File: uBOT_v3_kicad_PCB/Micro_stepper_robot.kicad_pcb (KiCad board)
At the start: 2 copper layers, 37 x 47 mm, 29 parts, among them J4 USB_B_Micro, M1 Stepper_Motor_bipolar, M2 Stepper_Motor_bipolar, M3 Stepper_Motor_bipolar, M4 Stepper_Motor_bipolar, SW3 EN, SW4 BOOT, U1 DRV8833PW, U2 TCRT5000, U4 ESP32-WROOM-32D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

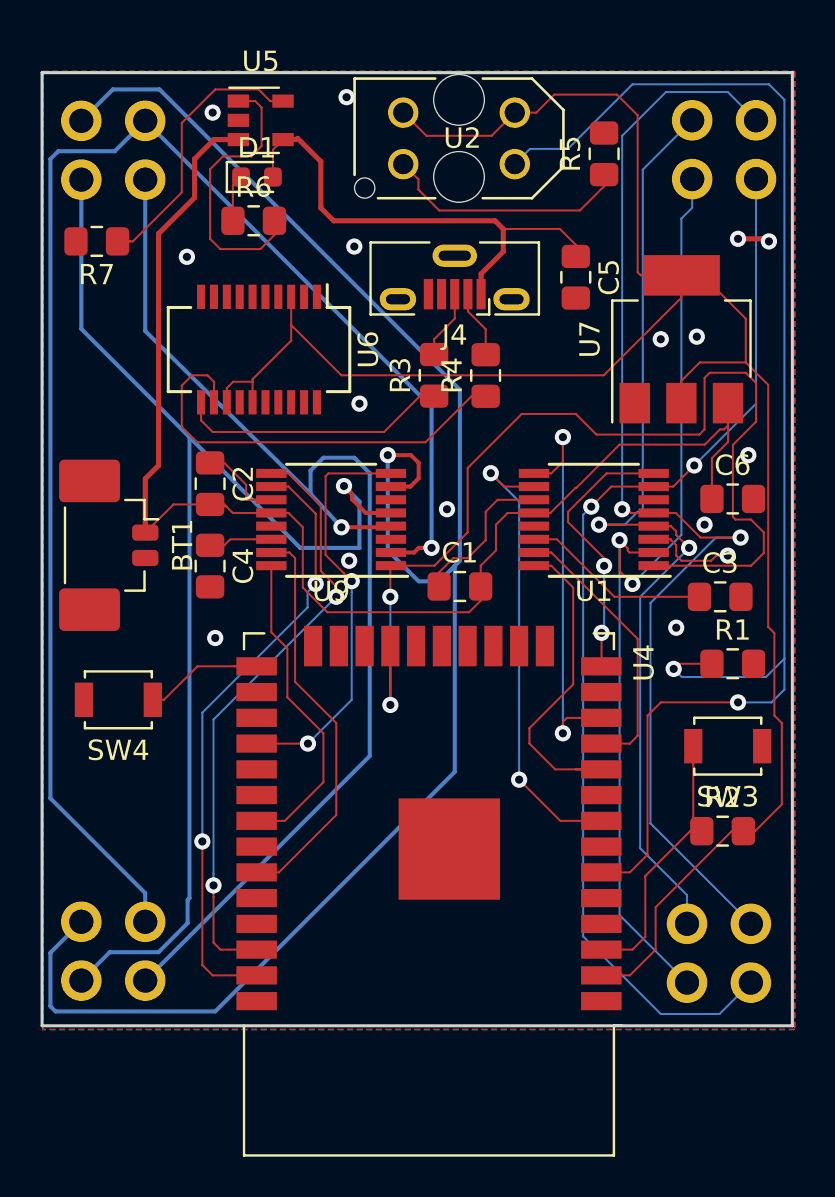
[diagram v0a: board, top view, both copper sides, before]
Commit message: added filter caps to 3.3v and VBAT
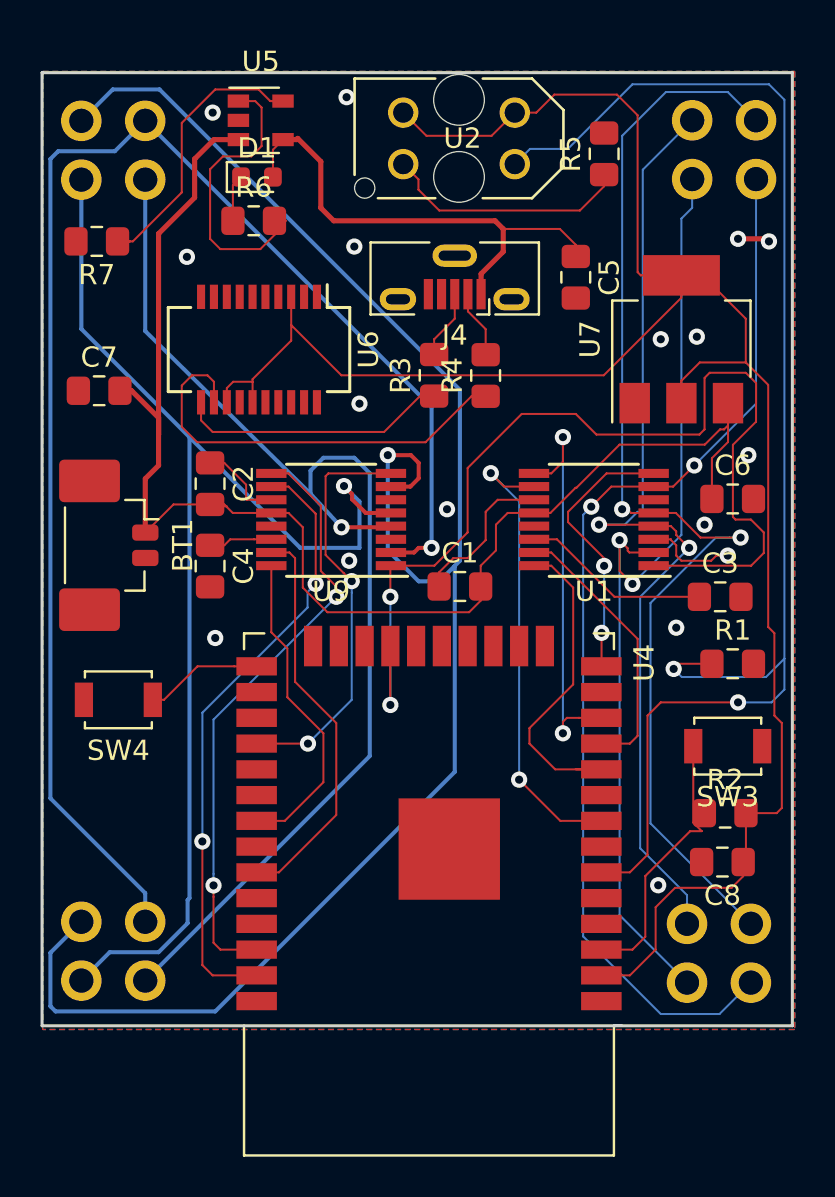
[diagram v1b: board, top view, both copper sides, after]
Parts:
- added C7: 10uF, Capacitor_SMD:C_0805_2012Metric_Pad1.15x1.40mm_HandSolder, F.Cu at (105.7, 68.3)
- added C8: 10uF, Capacitor_SMD:C_0805_2012Metric_Pad1.15x1.40mm_HandSolder, F.Cu at (136.4, 91.6)
- C3, C4: value C_Small -> 2.2uF
- moved R2 0.90 mm to (136.5, 89.2)
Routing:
- net +BATT: track 67.7 -> 71.0 mm
- net +3V3: track 101.3 -> 103.2 mm
- net GND: vias 16 -> 17
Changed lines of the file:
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@@
     (thickness 1.6)
     (drawings 5)
-    (tracks 467)
+    (tracks 476)
     (zones 0)
-    (modules 29)
+    (modules 31)
     (nets 73)
   )
@@
     (add_net "Net-(U6-Pad9)")
   )
+  (module Capacitor_SMD:C_0805_2012Metric_Pad1.15x1.40mm_HandSolder (layer F.Cu)
+    (at 136.389 91.567 180)
+    (descr "Capacitor SMD 0805 (2012 Metric), square (rectangular) end terminal, IPC_7351 nominal with elongated pad for handsoldering. (Body size source: https://docs.google.com/spreadsheets/d/1BsfQQcO9C6DZCsRaXUlFlo91Tg2WpOkGARC1WS5S8t0/edit?usp=sharing), generated with kicad-footprint-generator")
+    (tags "capacitor handsolder")
+    (attr smd)
+    (fp_text reference C8 (at 0 -1.65) (layer F.SilkS)
+      (effects (font (size 1 1) (thickness 0.15)))
+    )
+    (fp_text value 10uF (at 0 1.65) (layer F.Fab)
+      (effects (font (size 1 1) (thickness 0.15)))
+    )
+    (fp_text user %R (at 0 0) (layer F.Fab)
+      (effects (font (size 0.5 0.5) (thickness 0.08)))
+    )
+    (fp_line (start 1.85 0.95) (end -1.85 0.95) (layer F.CrtYd) (width 0.05))
+    (fp_line (start 1.85 -0.95) (end 1.85 0.95) (layer F.CrtYd) (width 0.05))
+    (fp_line (start -1.85 -0.95) (end 1.85 -0.95) (layer F.CrtYd) (width 0.05))
+    (fp_line (start -1.85 0.95) (end -1.85 -0.95) (layer F.CrtYd) (width 0.05))
+    (fp_line (start -0.261252 0.71) (end 0.261252 0.71) (layer F.SilkS) (width 0.12))
+    (fp_line (start -0.261252 -0.71) (end 0.261252 -0.71) (layer F.SilkS) (width 0.12))
+    (fp_line (start 1 0.6) (end -1 0.6) (layer F.Fab) (width 0.1))
+    (fp_line (start 1 -0.6) (end 1 0.6) (layer F.Fab) (width 0.1))
+    (fp_line (start -1 -0.6) (end 1 -0.6) (layer F.Fab) (width 0.1))
+    (fp_line (start -1 0.6) (end -1 -0.6) (layer F.Fab) (width 0.1))
+    (pad 2 smd roundrect (at 1.025 0 180) (size 1.15 1.4) (layers F.Cu F.Paste F.Mask) (roundrect_rratio 0.217391)
+      (net 5 GND))
+    (pad 1 smd roundrect (at -1.025 0 180) (size 1.15 1.4) (layers F.Cu F.Paste F.Mask) (roundrect_rratio 0.217391)
+      (net 22 +3V3))
+    (model ${KISYS3DMOD}/Capacitor_SMD.3dshapes/C_0805_2012Metric.wrl
+      (at (xyz 0 0 0))
+      (scale (xyz 1 1 1))
+      (rotate (xyz 0 0 0))
+    )
+  )
+  (module Capacitor_SMD:C_0805_2012Metric_Pad1.15x1.40mm_HandSolder (layer F.Cu)
+    (at 105.655 68.326)
+    (descr "Capacitor SMD 0805 (2012 Metric), square (rectangular) end terminal, IPC_7351 nominal with elongated pad for handsoldering. (Body size source: https://docs.google.com/spreadsheets/d/1BsfQQcO9C6DZCsRaXUlFlo91Tg2WpOkGARC1WS5S8t0/edit?usp=sharing), generated with kicad-footprint-generator")
+    (tags "capacitor handsolder")
+    (attr smd)
+    (fp_text reference C7 (at 0 -1.65) (layer F.SilkS)
+      (effects (font (size 1 1) (thickness 0.15)))
+    )
+    (fp_text value 10uF (at 0 1.65) (layer F.Fab)
+      (effects (font (size 1 1) (thickness 0.15)))
+    )
+    (fp_text user %R (at 0 0) (layer F.Fab)
+      (effects (font (size 0.5 0.5) (thickness 0.08)))
+    )
+    (fp_line (start 1.85 0.95) (end -1.85 0.95) (layer F.CrtYd) (width 0.05))
+    (fp_line (start 1.85 -0.95) (end 1.85 0.95) (layer F.CrtYd) (width 0.05))
+    (fp_line (start -1.85 -0.95) (end 1.85 -0.95) (layer F.CrtYd) (width 0.05))
+    (fp_line (start -1.85 0.95) (end -1.85 -0.95) (layer F.CrtYd) (width 0.05))
+    (fp_line (start -0.261252 0.71) (end 0.261252 0.71) (layer F.SilkS) (width 0.12))
+    (fp_line (start -0.261252 -0.71) (end 0.261252 -0.71) (layer F.SilkS) (width 0.12))
+    (fp_line (start 1 0.6) (end -1 0.6) (layer F.Fab) (width 0.1))
+    (fp_line (start 1 -0.6) (end 1 0.6) (layer F.Fab) (width 0.1))
+    (fp_line (start -1 -0.6) (end 1 -0.6) (layer F.Fab) (width 0.1))
+    (fp_line (start -1 0.6) (end -1 -0.6) (layer F.Fab) (width 0.1))
+    (pad 2 smd roundrect (at 1.025 0) (size 1.15 1.4) (layers F.Cu F.Paste F.Mask) (roundrect_rratio 0.217391)
+      (net 4 +BATT))
+    (pad 1 smd roundrect (at -1.025 0) (size 1.15 1.4) (layers F.Cu F.Paste F.Mask) (roundrect_rratio 0.217391)
+      (net 5 GND))
+    (model ${KISYS3DMOD}/Capacitor_SMD.3dshapes/C_0805_2012Metric.wrl
+      (at (xyz 0 0 0))
+      (scale (xyz 1 1 1))
+      (rotate (xyz 0 0 0))
+    )
+  )
   (module Connector_Molex:Molex_PicoBlade_53398-0271_1x02-1MP_P1.25mm_Vertical (layer F.Cu)
     (at 106.68 75.946 270)
@@
       (effects (font (size 1 1) (thickness 0.15)))
     )
-    (fp_text value C_Small (at 0 1.65) (layer F.Fab)
+    (fp_text value 2.2uF (at 0 1.65) (layer F.Fab)
       (effects (font (size 1 1) (thickness 0.15)))
     )
@@
       (effects (font (size 1 1) (thickness 0.15)))
     )
-    (fp_text value C_Small (at 0 1.65 90) (layer F.Fab)
+    (fp_text value 2.2uF (at 0 1.65 90) (layer F.Fab)
       (effects (font (size 1 1) (thickness 0.15)))
     )
@@
   )
   (module Resistor_SMD:R_0805_2012Metric_Pad1.15x1.40mm_HandSolder (layer F.Cu)
-    (at 136.398 90.043)
+    (at 136.525 89.154)
     (descr "Resistor SMD 0805 (2012 Metric), square (rectangular) end terminal, IPC_7351 nominal with elongated pad for handsoldering. (Body size source: https://docs.google.com/spreadsheets/d/1BsfQQcO9C6DZCsRaXUlFlo91Tg2WpOkGARC1WS5S8t0/edit?usp=sharing), generated with kicad-footprint-generator")
     (tags "resistor handsolder")
@@
   (segment (start 107.93 75.321) (end 107.93 72.664) (width 0.254) (layer F.Cu) (net 4))
   (segment (start 107.93 72.664) (end 108.585 72.009) (width 0.254) (layer F.Cu) (net 4))
-  (segment (start 108.585 72.009) (end 108.585 60.579) (width 0.254) (layer F.Cu) (net 4))
   (segment (start 108.585 60.579) (end 110.363 58.801) (width 0.254) (layer F.Cu) (net 4))
   (segment (start 110.363 58.801) (end 110.363 56.896) (width 0.254) (layer F.Cu) (net 4))
@@
   (segment (start 114.994 74.351) (end 115.697 75.054) (width 0.1) (layer F.Cu) (net 4))
   (segment (start 115.697 75.054) (end 115.697 78.030004) (width 0.1) (layer F.Cu) (net 4))
+  (segment (start 108.585 69.656) (end 108.585 70.485) (width 0.254) (layer F.Cu) (net 4))
+  (segment (start 107.255 68.326) (end 108.585 69.656) (width 0.254) (layer F.Cu) (net 4))
+  (segment (start 106.68 68.326) (end 107.255 68.326) (width 0.254) (layer F.Cu) (net 4))
+  (segment (start 108.585 72.009) (end 108.585 70.485) (width 0.254) (layer F.Cu) (net 4))
+  (segment (start 108.585 70.485) (end 108.585 60.579) (width 0.254) (layer F.Cu) (net 4))
   (via (at 118.237 61.214) (size 0.8) (drill 0.4) (layers F.Cu B.Cu) (net 5))
   (via (at 111.379 80.518) (size 0.8) (drill 0.4) (layers F.Cu B.Cu) (net 5))
@@
   (segment (start 137.16 60.833) (end 138.557 60.833) (width 0.254) (layer F.Cu) (net 5))
   (via (at 117.856 53.848) (size 0.8) (drill 0.4) (layers F.Cu B.Cu) (net 5))
+  (via (at 133.223 92.71) (size 0.8) (drill 0.4) (layers F.Cu B.Cu) (net 5))
   (segment (start 122.419 77.278) (end 123.116 76.581) (width 0.1) (layer F.Cu) (net 6))
   (segment (start 122.419 77.978) (end 122.419 77.278) (width 0.1) (layer F.Cu) (net 6))
@@
   (segment (start 134.366 68.936) (end 134.366 67.836) (width 0.1) (layer F.Cu) (net 22))
   (segment (start 135.273 66.929) (end 137.541 66.929) (width 0.1) (layer F.Cu) (net 22))
-  (segment (start 138.64701 68.03501) (end 138.64701 79.97301) (width 0.1) (layer F.Cu) (net 22))
-  (segment (start 137.541 66.929) (end 138.64701 68.03501) (width 0.1) (layer F.Cu) (net 22))
-  (segment (start 138.952001 80.278001) (end 138.952001 84.342001) (width 0.1) (layer F.Cu) (net 22))
-  (segment (start 138.64701 79.97301) (end 138.952001 80.278001) (width 0.1) (layer F.Cu) (net 22))
-  (segment (start 138.952001 84.342001) (end 139.319 84.709) (width 0.1) (layer F.Cu) (net 22))
-  (segment (start 137.998 90.043) (end 137.423 90.043) (width 0.1) (layer F.Cu) (net 22))
-  (segment (start 139.319 88.722) (end 137.998 90.043) (width 0.1) (layer F.Cu) (net 22))
-  (segment (start 139.319 84.709) (end 139.319 88.722) (width 0.1) (layer F.Cu) (net 22))
-  (segment (start 136.848 90.043) (end 133.096 93.795) (width 0.1) (layer F.Cu) (net 22))
-  (segment (start 137.423 90.043) (end 136.848 90.043) (width 0.1) (layer F.Cu) (net 22))
   (segment (start 133.096 93.795) (end 133.096 95.885) (width 0.1) (layer F.Cu) (net 22))
   (segment (start 131.826 97.155) (end 130.42 97.155) (width 0.1) (layer F.Cu) (net 22))
@@
   (segment (start 137.541 64.77) (end 137.541 66.929) (width 0.1) (layer F.Cu) (net 22))
   (segment (start 135.407 62.636) (end 137.541 64.77) (width 0.1) (layer F.Cu) (net 22))
+  (segment (start 139.065 89.154) (end 137.55 89.154) (width 0.1) (layer F.Cu) (net 22))
+  (segment (start 139.319 88.9) (end 139.065 89.154) (width 0.1) (layer F.Cu) (net 22))
+  (segment (start 139.319 84.709) (end 139.319 88.9) (width 0.1) (layer F.Cu) (net 22))
+  (segment (start 138.64701 68.03501) (end 138.64701 79.97301) (width 0.1) (layer F.Cu) (net 22))
+  (segment (start 137.541 66.929) (end 138.64701 68.03501) (width 0.1) (layer F.Cu) (net 22))
+  (segment (start 138.64701 79.97301) (end 138.952001 80.278001) (width 0.1) (layer F.Cu) (net 22))
+  (segment (start 138.952001 84.342001) (end 139.319 84.709) (width 0.1) (layer F.Cu) (net 22))
+  (segment (start 138.952001 80.278001) (end 138.952001 84.342001) (width 0.1) (layer F.Cu) (net 22))
+  (segment (start 137.55 91.431) (end 137.414 91.567) (width 0.1) (layer F.Cu) (net 22))
+  (segment (start 137.55 89.154) (end 137.55 91.431) (width 0.1) (layer F.Cu) (net 22))
+  (segment (start 137.414 92.267) (end 136.844 92.837) (width 0.1) (layer F.Cu) (net 22))
+  (segment (start 137.414 91.567) (end 137.414 92.267) (width 0.1) (layer F.Cu) (net 22))
+  (segment (start 134.054 92.837) (end 133.096 93.795) (width 0.1) (layer F.Cu) (net 22))
+  (segment (start 136.844 92.837) (end 134.054 92.837) (width 0.1) (layer F.Cu) (net 22))
   (segment (start 121.474 68.589) (end 119.705 70.358) (width 0.1) (layer F.Cu) (net 23))
   (segment (start 122.174 68.589) (end 121.474 68.589) (width 0.1) (layer F.Cu) (net 23))
